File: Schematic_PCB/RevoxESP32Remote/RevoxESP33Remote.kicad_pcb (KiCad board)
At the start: 2 copper layers, 26 parts, among them J1 Conn_01x06, J1 Conn_01x08, J2 Conn_01x04, J2 Conn_01x06, J3 Conn_01x10, J4 Conn_01x05, J5 Conn_01x02, J5 Conn_01x04, J6 Conn_01x03, J7 Conn_01x03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

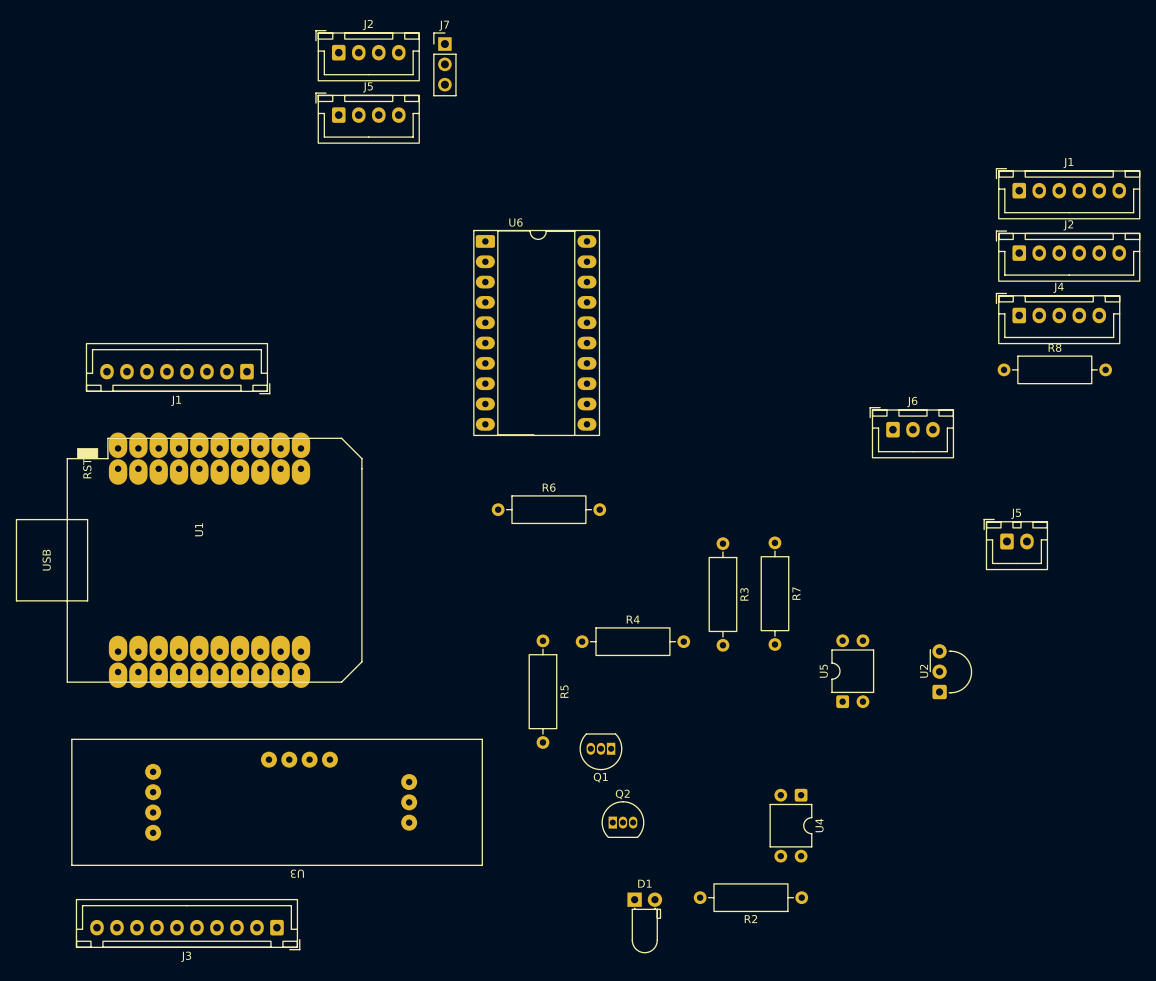
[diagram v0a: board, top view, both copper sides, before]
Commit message: IR Codes für Tape1, Tape2, Amplifier, B203, Phono und CD PLayer ergänzt.
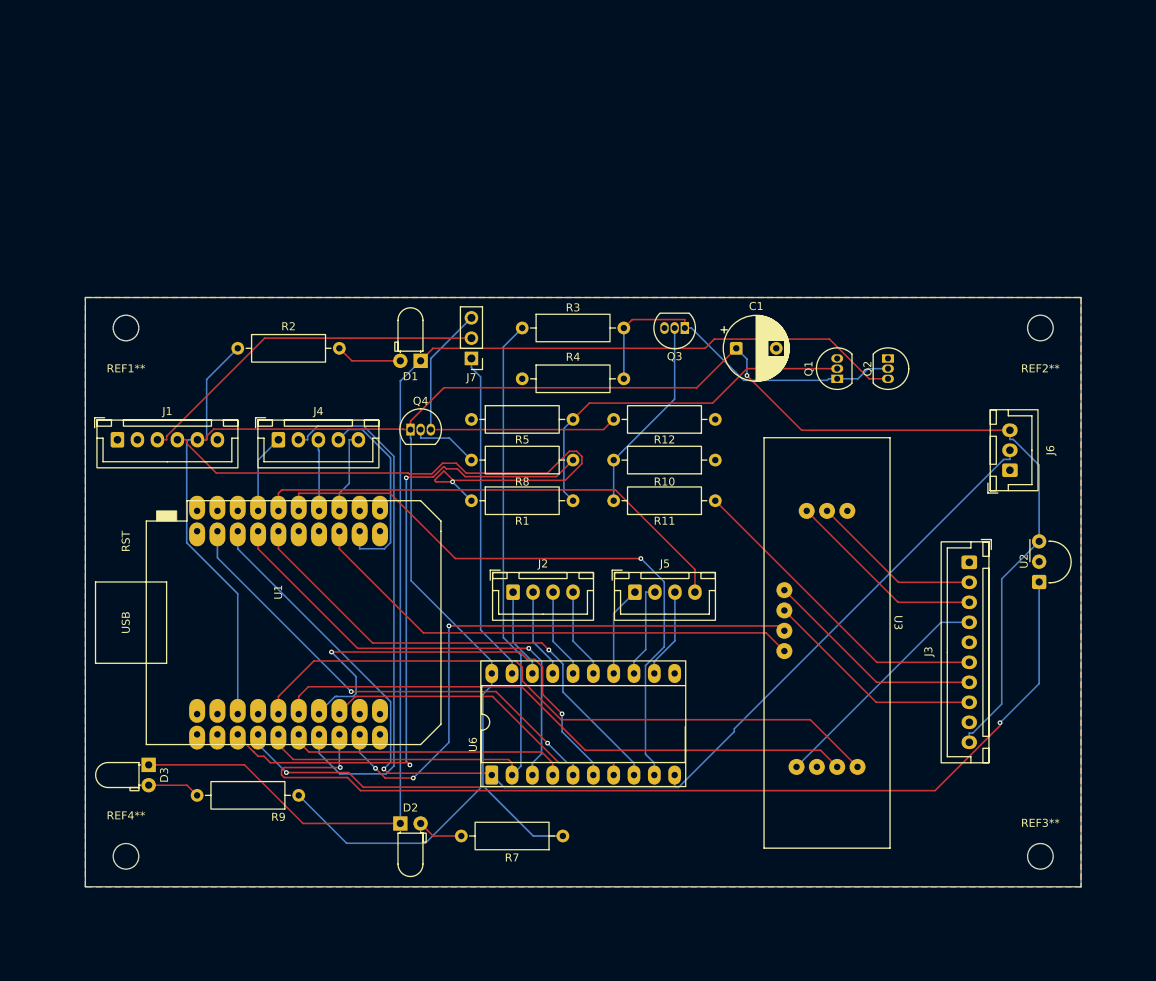
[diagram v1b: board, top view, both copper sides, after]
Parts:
- removed the J1 at (102.8, 71.5)
- removed the J1 at (199.3, 48.9)
- removed the J2 at (199.3, 56.7)
- removed the J2 at (114.2, 31.6)
- removed the J5 at (114.2, 39.4)
- removed the J5 at (197.8, 92.7)
- removed R6: 4,7k, Resistor_THT:R_Axial_DIN0309_L9.0mm_D3.2mm_P12.70mm_Horizontal
- removed U4, U5: AQY280EH, Package_DIP:DIP-4_W7.62mm
- added C1: 1000uF/16V, Capacitor_THT:CP_Radial_D8.0mm_P5.00mm, F.Cu at (163.9, 68.6)
- added D2: LED, LED_THT:LED_D3.0mm_Horizontal_O1.27mm_Z2.0mm_IRBlack, F.Cu at (121.9, 128.0)
- added D3: LED, LED_THT:LED_D3.0mm_Horizontal_O1.27mm_Z2.0mm_IRBlack, F.Cu at (90.5, 120.7)
- added J1: SerialLink, Connector_JST:JST_XH_B6B-XH-A_1x06_P2.50mm_Vertical, F.Cu at (86.6, 80.0)
- added J2: Conn_01x04, Connector_JST:JST_XH_B4B-XH-A_1x04_P2.50mm_Vertical, F.Cu at (136.0, 99.1)
- added J5: Conn_01x04, Connector_JST:JST_XH_B4B-XH-A_1x04_P2.50mm_Vertical, F.Cu at (151.2, 99.1)
- added Q3: BC550, Package_TO_SOT_THT:TO-92_Inline, F.Cu at (157.5, 66.0)
- added Q4: BC550, Package_TO_SOT_THT:TO-92_Inline, F.Cu at (123.2, 78.7)
- added R1: 4,7k, Resistor_THT:R_Axial_DIN0309_L9.0mm_D3.2mm_P12.70mm_Horizontal, F.Cu at (130.8, 87.6)
- added R10: 22k, Resistor_THT:R_Axial_DIN0309_L9.0mm_D3.2mm_P12.70mm_Horizontal, F.Cu at (161.3, 82.5)
- added R11: 4,7k, Resistor_THT:R_Axial_DIN0309_L9.0mm_D3.2mm_P12.70mm_Horizontal, F.Cu at (161.3, 87.6)
- added R12: 10k, Resistor_THT:R_Axial_DIN0309_L9.0mm_D3.2mm_P12.70mm_Horizontal, F.Cu at (161.3, 77.5)
- added R9: 180, Resistor_THT:R_Axial_DIN0309_L9.0mm_D3.2mm_P12.70mm_Horizontal, F.Cu at (109.2, 124.5)
- added REF1**: MountingHole_3.2mm_M3, MountingHole:MountingHole_3.2mm_M3, F.Cu at (87.6, 66.0)
- added REF2**: MountingHole_3.2mm_M3, MountingHole:MountingHole_3.2mm_M3, F.Cu at (201.9, 66.0)
- added REF3**: MountingHole_3.2mm_M3, MountingHole:MountingHole_3.2mm_M3, F.Cu at (201.9, 132.1)
- added REF4**: MountingHole_3.2mm_M3, MountingHole:MountingHole_3.2mm_M3, F.Cu at (87.6, 132.1)
- R7: value 460R -> 180
- R8: value 460R -> 10k
- moved R2 98.4 mm to (101.6, 68.6), turned to 0 degrees
- moved J3 97.9 mm to (193.0, 95.3), turned to -90 degrees
- moved J4 93.9 mm to (106.7, 80.0)
- moved D1 72.5 mm to (124.5, 70.1), turned to 180 degrees
- moved U3 69.9 mm to (175.3, 102.9), turned to -90 degrees
- moved Q2 67.4 mm to (182.9, 69.8), turned to -90 degrees
- moved U6 66.7 mm to (133.3, 121.9), turned to 90 degrees
- moved R8 55.0 mm to (143.5, 82.5), turned to 180 degrees
- moved Q1 54.2 mm to (176.5, 72.4), turned to 90 degrees
- moved R7 45.2 mm to (142.2, 129.5), turned to 180 degrees
- moved J7 39.4 mm to (130.8, 69.8), turned to 180 degrees
- moved R3 36.8 mm to (137.2, 66.0), turned to 0 degrees
- moved R4 33.7 mm to (137.2, 72.4)
- moved R5 29.1 mm to (130.8, 77.5), turned to 0 degrees
- moved U2 18.5 mm to (201.8, 97.8)
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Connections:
- net RevoxSerial_RXD renamed RevoxTTL_RXD
- net RevoxSerial_TXD renamed RevoxTTL_TXD
- J3 pad 1: unconnected-(J3-Pin_1-Pad1) -> GND
- J3 pad 10: 232_RTS -> +5V
- J3 pad 2: GND -> RevoxRS232_TXD
- J3 pad 3: RS232_TXD -> RevoxRS232_RXD
- J3 pad 4: RS232_RXD -> RS232 +5V
- J3 pad 5: unconnected-(J3-Pin_5-Pad5) -> GND
- J3 pad 6: unconnected-(J3-Pin_6-Pad6) -> ~{EN2}
- J3 pad 7: RS232 +5V -> RS232_RTS
- J3 pad 8: +5V -> RS232_CTS
- J3 pad 9: 232_CTS -> unconnected-(J3-Pin_9-Pad9)
- R7 pad 1: IO04 -> +5V
- U3 pad 10: RS232_TXD -> RevoxRS232_TXD
- U3 pad 7: 232_CTS -> RS232_CTS
- U3 pad 8: 232_RTS -> RS232_RTS
- U3 pad 9: RS232_RXD -> RevoxRS232_RXD
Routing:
- net +5V: track 0.00 -> 299.9 mm, vias 0 -> 1
- net Net-(D1-K): track 0.00 -> 155.1 mm
- net +3V3: track 0.00 -> 135.6 mm, vias 0 -> 1
- net IRrecv: track 0.00 -> 126.2 mm, vias 0 -> 2
- net IO04: track 0.00 -> 91.2 mm
- net RevoxTTL_RXD: track 0.00 -> 82.9 mm
- net IO02: track 0.00 -> 82.1 mm, vias 0 -> 2
- net ~{EN1}: track 0.00 -> 81.8 mm, vias 0 -> 1
- net IO33: track 0.00 -> 78.1 mm, vias 0 -> 1
- net RevoxTTL_TXD: track 0.00 -> 74.2 mm
- net TTL_RTS: track 0.00 -> 73.3 mm, vias 0 -> 3
- net IO32: track 0.00 -> 66.4 mm
- net TTL_CTS: track 0.00 -> 63.1 mm
- net IO34: track 0.00 -> 61.4 mm
- net IO23: track 0.00 -> 61.3 mm, vias 0 -> 1
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- added copper zone on B.Cu, net GND
- added copper zone on F.Cu, net GND
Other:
- board outline added: 124.5 x 73.7 mm

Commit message: Bugfix wrong RXD/TXD pins.
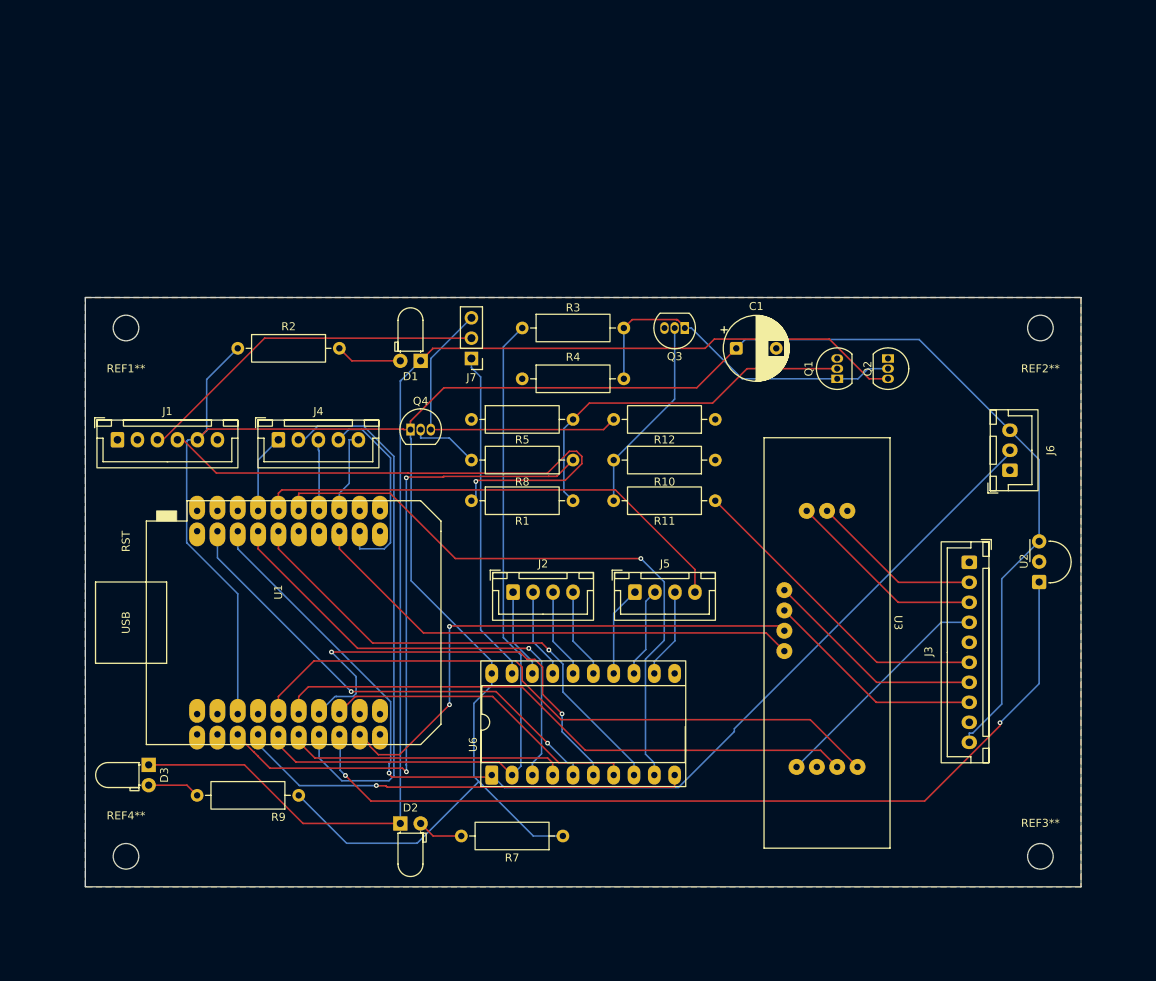
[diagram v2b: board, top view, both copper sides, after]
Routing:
- net IRrecv: track 126.2 -> 112.5 mm
- net ~{EN1}: track 81.8 -> 71.4 mm
- net TTL_RTS: track 73.3 -> 66.9 mm, vias 3 -> 2
- net IO32: track 66.4 -> 67.9 mm
- net IO04: track 91.2 -> 90.3 mm
- net +3V3: track 135.6 -> 134.8 mm
- net Net-(Q1-C): track 44.2 -> 43.5 mm
- net B6_TTL5V: track 11.9 -> 11.2 mm
- net +5V: track 299.9 -> 299.8 mm, vias 1 -> 0
